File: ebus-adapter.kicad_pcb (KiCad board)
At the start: 2 copper layers, 26.7 x 45.7 mm, 27 parts, among them Q1 BC817, Q2 BC817, Q3 BC817, U1 LM358DR, U2 FODM217C, U3 FODM217C

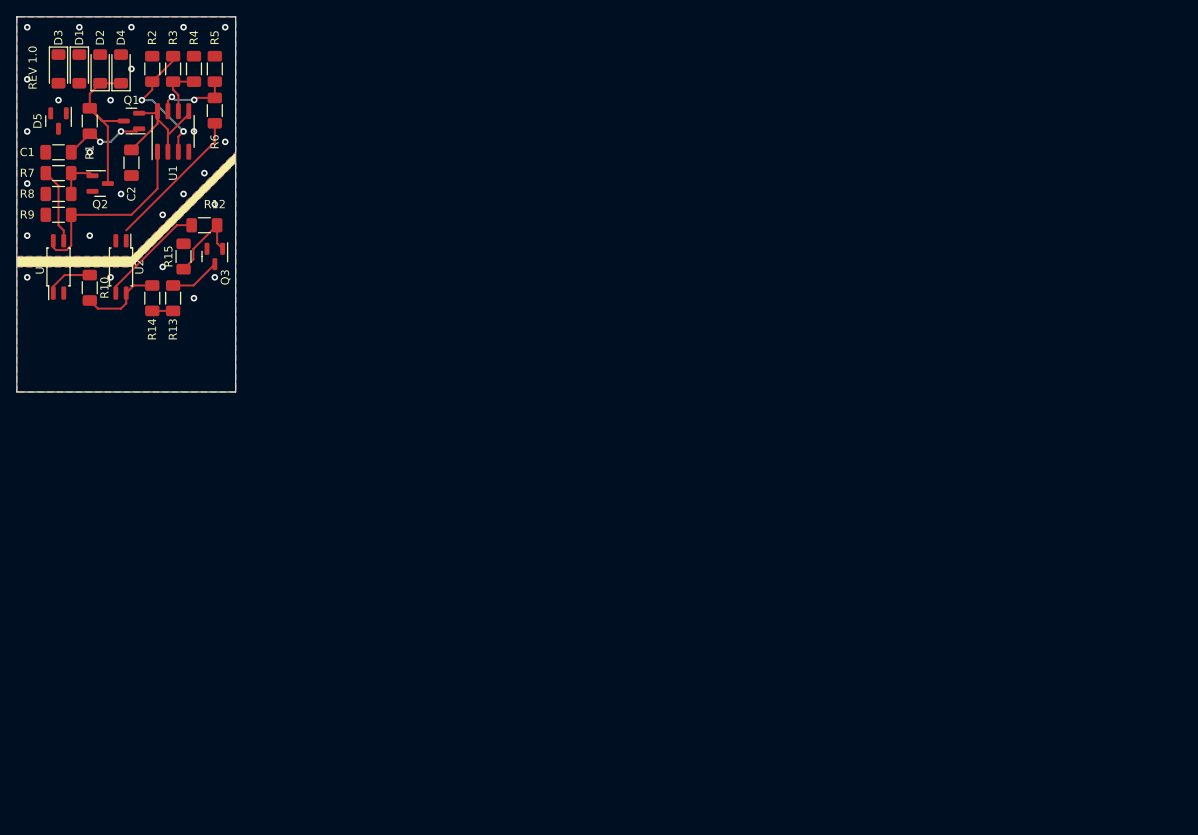
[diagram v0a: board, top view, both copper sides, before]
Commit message: Updated adapter added SPI 2 Etherenet adapter
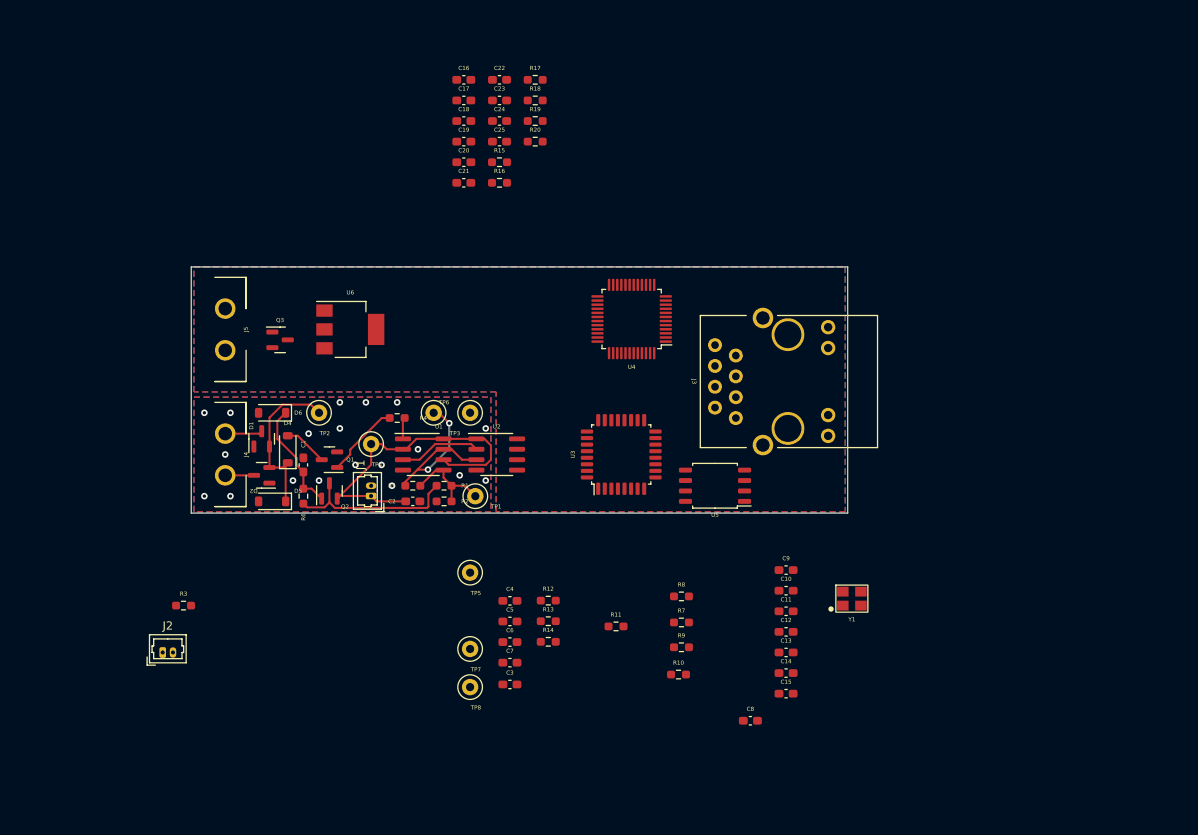
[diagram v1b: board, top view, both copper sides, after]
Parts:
- removed D3: D, Diode_SMD:D_MiniMELF
- added C10: 100u, Capacitor_SMD:C_0603_1608Metric_Pad1.08x0.95mm_HandSolder, F.Cu at (172.5, 94.1)
- added C11: 10u, Capacitor_SMD:C_0603_1608Metric_Pad1.08x0.95mm_HandSolder, F.Cu at (172.5, 96.6)
- added C12: 100p, Capacitor_SMD:C_0603_1608Metric_Pad1.08x0.95mm_HandSolder, F.Cu at (172.5, 99.1)
- added C13: 18p, Capacitor_SMD:C_0603_1608Metric_Pad1.08x0.95mm_HandSolder, F.Cu at (172.5, 101.6)
- added C14: 18p, Capacitor_SMD:C_0603_1608Metric_Pad1.08x0.95mm_HandSolder, F.Cu at (172.5, 104.1)
- added C15: 10n, Capacitor_SMD:C_0603_1608Metric_Pad1.08x0.95mm_HandSolder, F.Cu at (172.5, 106.6)
- added C16: 10n, Capacitor_SMD:C_0603_1608Metric_Pad1.08x0.95mm_HandSolder, F.Cu at (133.2, 31.8)
- added C17: 10n, Capacitor_SMD:C_0603_1608Metric_Pad1.08x0.95mm_HandSolder, F.Cu at (133.2, 34.3)
- added C18: 10u, Capacitor_SMD:C_0603_1608Metric_Pad1.08x0.95mm_HandSolder, F.Cu at (133.2, 36.8)
- added C19: 22n, Capacitor_SMD:C_0603_1608Metric_Pad1.08x0.95mm_HandSolder, F.Cu at (133.2, 39.3)
- added C20: 6.8n, Capacitor_SMD:C_0603_1608Metric_Pad1.08x0.95mm_HandSolder, F.Cu at (133.2, 41.9)
- added C21: 6.8n, Capacitor_SMD:C_0603_1608Metric_Pad1.08x0.95mm_HandSolder, F.Cu at (133.2, 44.4)
- added C22: 10n, Capacitor_SMD:C_0603_1608Metric_Pad1.08x0.95mm_HandSolder, F.Cu at (137.6, 31.8)
- added C23: 1n/2kV, Capacitor_SMD:C_0603_1608Metric_Pad1.08x0.95mm_HandSolder, F.Cu at (137.6, 34.3)
- added C24: C, Capacitor_SMD:C_0603_1608Metric_Pad1.08x0.95mm_HandSolder, F.Cu at (137.6, 36.8)
- added C25: C, Capacitor_SMD:C_0603_1608Metric_Pad1.08x0.95mm_HandSolder, F.Cu at (137.6, 39.3)
- added C3: 10u, Capacitor_SMD:C_0603_1608Metric_Pad1.08x0.95mm_HandSolder, F.Cu at (138.8, 105.5)
- added C4: 100u, Capacitor_SMD:C_0603_1608Metric_Pad1.08x0.95mm_HandSolder, F.Cu at (138.8, 95.3)
- added C5: 100p, Capacitor_SMD:C_0603_1608Metric_Pad1.08x0.95mm_HandSolder, F.Cu at (138.8, 97.8)
- added C6: 100u, Capacitor_SMD:C_0603_1608Metric_Pad1.08x0.95mm_HandSolder, F.Cu at (138.8, 100.3)
- added C7: 10u, Capacitor_SMD:C_0603_1608Metric_Pad1.08x0.95mm_HandSolder, F.Cu at (138.8, 102.8)
- added C8: 100p, Capacitor_SMD:C_0603_1608Metric_Pad1.08x0.95mm_HandSolder, F.Cu at (168.1, 109.9)
- added C9: 4.7u, Capacitor_SMD:C_0603_1608Metric_Pad1.08x0.95mm_HandSolder, F.Cu at (172.5, 91.6)
- added D6: 3.9V, Diode_SMD:D_SOD-123, F.Cu at (109.9, 72.4)
- added J1: Conn_01x02_Socket, Connector_Molex:Molex_PicoBlade_53047-0210_1x02_P1.25mm_Vertical, F.Cu at (121.9, 82.5)
- added J2: Conn_01x02_Socket, Connector_Molex:Molex_PicoBlade_53047-0210_1x02_P1.25mm_Vertical, F.Cu at (96.5, 101.6)
- added J3: HR911105A, ebus-adapter-footprints:HR911105A, F.Cu at (172.7, 68.6)
- added J4: WJ2EDGRC-5.08-2P, ebus-adapter-footprints:WJ2EDGRC, F.Cu at (104.1, 77.5)
- added J5: PWR, ebus-adapter-footprints:WJ2EDGRC, F.Cu at (104.1, 62.2)
- added R11: 0, Resistor_SMD:R_0603_1608Metric_Pad0.98x0.95mm_HandSolder, F.Cu at (151.8, 98.4)
- added R16: 49.9 1%, Resistor_SMD:R_0603_1608Metric_Pad0.98x0.95mm_HandSolder, F.Cu at (137.6, 44.4)
- added R17: 10 1%, Resistor_SMD:R_0603_1608Metric_Pad0.98x0.95mm_HandSolder, F.Cu at (141.9, 31.8)
- added R18: 49.9 1%, Resistor_SMD:R_0603_1608Metric_Pad0.98x0.95mm_HandSolder, F.Cu at (141.9, 34.3)
- added R19: 49.9 1%, Resistor_SMD:R_0603_1608Metric_Pad0.98x0.95mm_HandSolder, F.Cu at (141.9, 36.8)
- added R20: 10k, Resistor_SMD:R_0603_1608Metric_Pad0.98x0.95mm_HandSolder, F.Cu at (141.9, 39.3)
- added TP1: EBUS_RX, TestPoint:TestPoint_Loop_D1.80mm_Drill1.0mm_Beaded, F.Cu at (134.6, 82.5)
- added TP2: EBUS_SIG, TestPoint:TestPoint_Loop_D1.80mm_Drill1.0mm_Beaded, F.Cu at (115.6, 72.4)
- added TP3: EBUS_RX_LL, TestPoint:TestPoint_Loop_D1.80mm_Drill1.0mm_Beaded, F.Cu at (129.5, 72.4)
- added TP4: EBUS_3.3, TestPoint:TestPoint_Loop_D1.80mm_Drill1.0mm_Beaded, F.Cu at (121.9, 76.2)
- added TP5: BOOT0, TestPoint:TestPoint_Loop_D1.80mm_Drill1.0mm_Beaded, F.Cu at (134.0, 91.9)
- added TP6: GND1, TestPoint:TestPoint_Loop_D1.80mm_Drill1.0mm_Beaded, F.Cu at (134.0, 72.4)
- added TP7: GND2, TestPoint:TestPoint_Loop_D1.80mm_Drill1.0mm_Beaded, F.Cu at (134.0, 101.2)
- added TP8: 3.3V, TestPoint:TestPoint_Loop_D1.80mm_Drill1.0mm_Beaded, F.Cu at (134.0, 105.8)
- added U4: W5500, Package_QFP:LQFP-48_7x7mm_P0.5mm, F.Cu at (153.7, 61.0)
- added U5: W25Q128JVSIQ, Package_SO:SOIC-8_5.23x5.23mm_P1.27mm, F.Cu at (163.8, 81.3)
- added U6: AMS1117-3.3, Package_TO_SOT_SMD:SOT-223-3_TabPin2, F.Cu at (119.4, 62.2)
- added Y1: YSX321SL @24Mhz, ebus-adapter-footprints:YSX321SL, F.Cu at (180.5, 95.0)
- C1, C2: footprint Capacitor_SMD:C_1206_3216Metric_Pad1.33x1.80mm_HandSolder -> Capacitor_SMD:C_0603_1608Metric_Pad1.08x0.95mm_HandSolder
- D1, D2: value D -> BAV99; footprint Diode_SMD:D_MiniMELF -> Package_TO_SOT_SMD:SOT-23
- D4: value D -> 7.5V/1W; footprint Diode_SMD:D_MiniMELF -> Diode_SMD:D_SOD-123
- D5: value 3.9V -> 24V/1W; footprint Package_TO_SOT_SMD:SOT-23 -> Diode_SMD:D_SOD-123
- Q3: value BC817 -> DMN13H750S
- R1, R5: footprint Resistor_SMD:R_1206_3216Metric_Pad1.30x1.75mm_HandSolder -> Resistor_SMD:R_0603_1608Metric_Pad0.98x0.95mm_HandSolder
- R10, R7: value R -> 10k; footprint Resistor_SMD:R_1206_3216Metric_Pad1.30x1.75mm_HandSolder -> Resistor_SMD:R_0603_1608Metric_Pad0.98x0.95mm_HandSolder
- R12: value 1k -> 10k; footprint Resistor_SMD:R_1206_3216Metric_Pad1.30x1.75mm_HandSolder -> Resistor_SMD:R_0603_1608Metric_Pad0.98x0.95mm_HandSolder
- R13: value 1k -> 12.4k 1%; footprint Resistor_SMD:R_1206_3216Metric_Pad1.30x1.75mm_HandSolder -> Resistor_SMD:R_0603_1608Metric_Pad0.98x0.95mm_HandSolder
- R14: value 10k -> 1M; footprint Resistor_SMD:R_1206_3216Metric_Pad1.30x1.75mm_HandSolder -> Resistor_SMD:R_0603_1608Metric_Pad0.98x0.95mm_HandSolder
- R15: value 10k -> 49.9 1%; footprint Resistor_SMD:R_1206_3216Metric_Pad1.30x1.75mm_HandSolder -> Resistor_SMD:R_0603_1608Metric_Pad0.98x0.95mm_HandSolder
- R2: value 173k -> 33k; footprint Resistor_SMD:R_1206_3216Metric_Pad1.30x1.75mm_HandSolder -> Resistor_SMD:R_0603_1608Metric_Pad0.98x0.95mm_HandSolder
- R3: value 33k -> R; footprint Resistor_SMD:R_1206_3216Metric_Pad1.30x1.75mm_HandSolder -> Resistor_SMD:R_0603_1608Metric_Pad0.98x0.95mm_HandSolder
- R4: value 67k -> 4k7; footprint Resistor_SMD:R_1206_3216Metric_Pad1.30x1.75mm_HandSolder -> Resistor_SMD:R_0603_1608Metric_Pad0.98x0.95mm_HandSolder
- R6: value R -> 100k; footprint Resistor_SMD:R_1206_3216Metric_Pad1.30x1.75mm_HandSolder -> Resistor_SMD:R_0603_1608Metric_Pad0.98x0.95mm_HandSolder
- R8, R9: value R -> 330; footprint Resistor_SMD:R_1206_3216Metric_Pad1.30x1.75mm_HandSolder -> Resistor_SMD:R_0603_1608Metric_Pad0.98x0.95mm_HandSolder
- U2: value FODM217C -> ADuM1201BR; footprint Package_SO:SOP-4_4.4x2.6mm_P1.27mm -> Package_SO:SOIC-8_3.9x4.9mm_P1.27mm
- U3: value FODM217C -> STM32L412KBTx; footprint Package_SO:SOP-4_4.4x2.6mm_P1.27mm -> Package_QFP:LQFP-32_7x7mm_P0.8mm
- moved R7 93.6 mm to (159.7, 97.9), turned to 0 degrees
- moved R9 92.4 mm to (159.7, 101.0), turned to 0 degrees
- moved R8 90.4 mm to (159.7, 94.8)
- moved R10 85.9 mm to (159.4, 104.3), turned to 0 degrees
- moved U3 72.3 mm to (152.4, 77.5)
- moved R3 65.4 mm to (99.1, 95.9), turned to 0 degrees
- moved R14 63.9 mm to (143.5, 100.3), turned to 0 degrees
- moved R2 63.6 mm to (130.8, 83.2), turned to 180 degrees
- moved R12 62.0 mm to (143.5, 95.3), turned to 0 degrees
- moved R1 62.0 mm to (130.8, 81.3), turned to 0 degrees
- moved R13 60.3 mm to (143.5, 97.8), turned to 0 degrees
- moved R5 56.2 mm to (127.0, 81.3), turned to 180 degrees
- moved C2 53.7 mm to (127.0, 83.2), turned to 0 degrees
- moved D2 53.3 mm to (108.6, 80.0), turned to 180 degrees
- moved D5 53.2 mm to (109.9, 83.2), turned to 180 degrees
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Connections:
- C1 pad 1: Net-(D5-K) -> Net-(D6-K)
- C1 pad 2: GNDPWR -> GND1
- C2 pad 1: EBUS_3.3_VREF -> /EBUS_3.3V
- C2 pad 2: GNDPWR -> GND1
- D1 pad 1: /Ebus-To-UART/EBUS1 -> GND1
- D1 pad 2: GNDPWR -> /EBUS_SIGNAL
- D2 pad 1: EBUS_SIGNAL -> GND1
- D2 pad 2: /Ebus-To-UART/EBUS1 -> /EBUS_SIGNAL
- D4 pad 1: EBUS_SIGNAL -> /EBUS_SIGNAL
- D4 pad 2: /Ebus-To-UART/EBUS2 -> Net-(D4-A)
- D5 pad 1: Net-(D5-K) -> /EBUS_SIGNAL
- D5 pad 2: GNDPWR -> GND1
- Q1 pad 1: Net-(D5-K) -> Net-(Q1-B)
- Q1 pad 2: EBUS_3.3_VREF -> GND1
- Q1 pad 3: EBUS_SIGNAL -> Net-(D4-A)
- Q2 pad 1: Net-(Q2-B) -> Net-(D6-K)
- Q2 pad 2: GNDPWR -> /EBUS_3.3V
- Q2 pad 3: EBUS_SIGNAL -> /EBUS_SIGNAL
- Q3 pad 1: Net-(Q3-B) -> GND2
- Q3 pad 2: GND -> Net-(Q3-S)
- Q3 pad 3: Net-(Q3-C) -> Net-(J5-In)
- R1 pad 1: EBUS_SIGNAL -> /EBUS_SIGNAL
- R1 pad 2: Net-(D5-K) -> Net-(U1B-+)
- R10 pad 1: Net-(R10-Pad1) -> +3.3V
- R10 pad 2: +3.3V -> /NRST_MCU
- R12 pad 1: Net-(Q3-B) -> +3.3V
- R12 pad 2: Net-(R12-Pad2) -> Net-(U4-PMODE0)
- R13 pad 1: /Ebus-To-UART/RX -> Net-(U4-EXRES1)
- R13 pad 2: Net-(Q3-C) -> GND2
- R14 pad 1: +3.3V -> Net-(U4-XI/CLKIN)
- R14 pad 2: /Ebus-To-UART/RX -> Net-(U4-XO)
- R15 pad 1: Net-(Q3-B) -> +3.3VA
- R15 pad 2: GND -> /TX-
- R2 pad 1: EBUS_SIGNAL -> Net-(U1B-+)
- R2 pad 2: Net-(U1A-+) -> GND1
- R3 pad 1: Net-(U1A-+) -> /_EBUS_PWR
- R3 pad 2: Net-(U1B--) -> Net-(D3-A)
- R4 pad 1: Net-(U1B--) -> Net-(R4-Pad1)
- R4 pad 2: GNDPWR -> Net-(Q1-B)
- R5 pad 1: Net-(U1B--) -> Net-(U1B-+)
- R5 pad 2: Net-(R5-Pad2) -> /VIB
- R6 pad 1: Net-(R5-Pad2) -> /EBUS_SIGNAL
- R6 pad 2: Net-(R6-Pad2) -> Net-(D6-K)
- R7 pad 1: Net-(Q2-B) -> +3.3V
- R7 pad 2: Net-(R7-Pad2) -> /NRST
- R8 pad 1: GNDPWR -> +3.3V
- R8 pad 2: Net-(Q2-B) -> Net-(J3-GLED-)
- R9 pad 1: Net-(R9-Pad1) -> Net-(J3-YLED-)
- R9 pad 2: GNDPWR -> +3.3V
- U1 pad 1: Net-(R9-Pad1) -> Net-(R4-Pad1)
- U1 pad 2: EBUS_3.3_VREF -> /EBUS_3.3V
- U1 pad 3: Net-(U1A-+) -> /VOA
- U1 pad 4: GNDPWR -> GND1
- U1 pad 5: EBUS_3.3_VREF -> Net-(U1B-+)
- U1 pad 6: Net-(U1B--) -> /EBUS_3.3V
- U1 pad 7: Net-(R5-Pad2) -> /VIB
- U1 pad 8: EBUS_3.3_VREF -> /EBUS_3.3V
- U2 pad 1: Net-(R6-Pad2) -> /EBUS_3.3V
- U2 pad 2: GNDPWR -> /VOA
- U2 pad 3: Net-(R12-Pad2) -> /VIB
- U2 pad 4: +3.3V -> GND1
- U3 pad 1: Net-(R10-Pad1) -> +3.3V
- U3 pad 2: /Ebus-To-UART/TX -> unconnected-(U3-PC14-Pad2)
- U3 pad 3: Net-(R7-Pad2) -> unconnected-(U3-PC15-Pad3)
- U3 pad 4: Net-(R9-Pad1) -> /NRST
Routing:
- net /EBUS_SIGNAL: track 0.00 -> 41.8 mm
- net /EBUS_3.3V: track 0.00 -> 40.9 mm
- net Net-(R9-Pad1): track 23.4 -> 0.00 mm
- net /VIB: track 0.00 -> 21.7 mm, vias 0 -> 2
- net EBUS_SIGNAL: track 21.0 -> 0.00 mm
- net EBUS_3.3_VREF: track 19.9 -> 0.00 mm
- net Net-(R6-Pad2): track 17.5 -> 0.00 mm
- net Net-(U1A-+): track 16.3 -> 0.00 mm, vias 2 -> 0
- net Net-(D6-K): track 0.00 -> 13.7 mm
- net Net-(R12-Pad2): track 13.1 -> 0.00 mm
- net Net-(U1B-+): track 0.00 -> 11.3 mm
- net Net-(D5-K): track 10.3 -> 0.00 mm, vias 2 -> 0
- net Net-(Q3-B): track 10.2 -> 0.00 mm
- net /VOA: track 0.00 -> 10.0 mm
- net +3.3V: track 9.93 -> 0.00 mm
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- added copper zone on B.Cu, net GND1
- added copper zone on F.Cu, net GND1
- added copper zone on B.Cu, net GND2
- added copper zone on F.Cu, net GND2
- removed copper zone on B.Cu, net GND
- removed copper zone on F.Cu, net GND
- removed copper zone on B.Cu, net GNDPWR
- removed copper zone on F.Cu, net GNDPWR
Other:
- board size 26.7 x 45.7 mm -> 80 x 30 mm
- board text removed: "REV 1.0"

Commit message: Updated schematics and pcb
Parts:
- removed C14: 18p, Capacitor_SMD:C_0603_1608Metric_Pad1.08x0.95mm_HandSolder
- removed C15, C22: 10n, Capacitor_SMD:C_0603_1608Metric_Pad1.08x0.95mm_HandSolder
- removed C19: 22n, Capacitor_SMD:C_0603_1608Metric_Pad1.08x0.95mm_HandSolder
- removed C20, C21: 6.8n, Capacitor_SMD:C_0603_1608Metric_Pad1.08x0.95mm_HandSolder
- removed R19: 49.9 1%, Resistor_SMD:R_0603_1608Metric_Pad0.98x0.95mm_HandSolder
- added D3: LED, LED_THT:LED_D1.8mm_W3.3mm_H2.4mm, F.Cu at (203.2, 73.7)
- added D7: LED, LED_THT:LED_D1.8mm_W3.3mm_H2.4mm, F.Cu at (210.8, 85.7)
- added FB1: 120 Ohm @ 100 MHz, Resistor_SMD:R_1206_3216Metric_Pad1.30x1.75mm_HandSolder, F.Cu at (129.8, 116.8)
- added FB2: 120 Ohm @ 100 MHz, Resistor_SMD:R_1206_3216Metric_Pad1.30x1.75mm_HandSolder, F.Cu at (148.4, 118.6)
- added J6: Conn_01x05_Pin, Connector_PinHeader_2.54mm:PinHeader_1x05_P2.54mm_Vertical, F.Cu at (113.7, 90.8)
- added J7: Conn_01x02_Socket, Connector_Molex:Molex_PicoBlade_53047-0210_1x02_P1.25mm_Vertical, F.Cu at (156.8, 92.7)
- added J8: Conn_01x02_Socket, Connector_Molex:Molex_PicoBlade_53047-0210_1x02_P1.25mm_Vertical, F.Cu at (217.8, 84.5)
- added SW2: PS-7054SVB-6PN, ebus-adapter-footprints:PS-7054SVB, F.Cu at (121.3, 97.2)
- C6: value 100u -> 10uF
- C7: value 10u -> 0.1uF
- C8: value 100p -> 0.1uF
- C9: value 4.7u -> 18p
- R12: value 10k -> 2.32k 1%
- R13: value 12.4k 1% -> 49.9 1%
- R14: value 1M -> 49.9 1%
- R17: value 10 1% -> 1M
- R18: value 49.9 1% -> R
- TP1, TP2, TP3, TP4, TP5, TP6, TP7, TP8: footprint TestPoint:TestPoint_Loop_D1.80mm_Drill1.0mm_Beaded -> TestPoint:TestPoint_THTPad_1.5x1.5mm_Drill0.7mm
- U4: value W5500 -> ENC28J60x-ML; footprint Package_QFP:LQFP-48_7x7mm_P0.5mm -> Package_DFN_QFN:QFN-28-1EP_6x6mm_P0.65mm_EP4.25x4.25mm
- Y1: value YSX321SL @24Mhz -> YSX321SL @25Mhz
- moved J2 112.2 mm to (204.1, 69.4)
- moved C17 81.3 mm to (133.0, 115.6)
- moved C18 80.6 mm to (133.0, 117.5)
- moved R17 73.1 mm to (137.2, 104.8), turned to -90 degrees
- moved R15 71.5 mm to (149.2, 112.4), turned to 180 degrees
- moved R16 71.1 mm to (149.2, 114.5), turned to 180 degrees
- moved C24 70.7 mm to (106.0, 100.1)
- moved C23 69.5 mm to (149.2, 102.9), turned to 180 degrees
- moved C16 68.7 mm to (143.5, 99.7), turned to 180 degrees
- moved C25 66.8 mm to (106.0, 98.2), turned to 180 degrees
- moved R18 64.4 mm to (155.9, 97.2)
- moved R20 63.7 mm to (128.3, 101.6), turned to -90 degrees
- moved TP6 56.0 mm to (103.5, 119.4)
- moved U4 52.1 mm to (142.2, 111.8), turned to 90 degrees
- moved C10 51.7 mm to (126.4, 117.5), turned to 180 degrees
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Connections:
- C13 pad 1: Net-(U4-XI/CLKIN) -> Net-(C13-Pad1)
- C6 pad 1: +3.3V -> Net-(U4-VCAP)
- C7 pad 1: +3.3V -> GND2
- C7 pad 2: GND2 -> Net-(J3-TCT)
- C8 pad 1: +3.3V -> GND2
- C8 pad 2: GND2 -> Net-(J3-RCT)
- C9 pad 1: Net-(U4-TOCAP) -> Net-(U4-OSC1)
- J1 pad 1: /EBUS_3.3V -> Net-(J1-Pin_1)
- J3 pad 3: Net-(J3-RXD+) -> /RX+
- J3 pad 6: Net-(J3-RXD-) -> /RX-
- R12 pad 1: +3.3V -> Net-(U4-RBIAS)
- R12 pad 2: Net-(U4-PMODE0) -> GND2
- R13 pad 1: Net-(U4-EXRES1) -> Net-(J3-RCT)
- R13 pad 2: GND2 -> /RX+
- R14 pad 1: Net-(U4-XI/CLKIN) -> Net-(J3-RCT)
- R14 pad 2: Net-(U4-XO) -> /RX-
- R15 pad 1: +3.3VA -> Net-(J3-TCT)
- R15 pad 2: /TX- -> /TX+
- R16 pad 1: +3.3VA -> Net-(J3-TCT)
- R16 pad 2: /TX+ -> /TX-
- R17 pad 1: +3.3VA -> Net-(C13-Pad1)
- R17 pad 2: Net-(J3-TCT) -> Net-(U4-OSC2)
- R18 pad 1: /RX+ -> /ACT
- R18 pad 2: Net-(J3-RCT) -> Net-(J7-Pin_1)
- R3 pad 1: /_EBUS_PWR -> /EBUS_3.3V
- R3 pad 2: Net-(D3-A) -> Net-(J1-Pin_1)
- U3 pad 10: unconnected-(U3-PA4-Pad10) -> /ACT
- U3 pad 21: /SPI_MISO -> /ETHER_DI
- U3 pad 22: /SPI_MOSI -> /ETHER_DO
- U3 pad 7: /SPI_SCK -> /ETHER_SCK
- U4 pad 1: /TX- -> unconnected-(U4-~{WOL}-Pad1)
- U4 pad 10: Net-(U4-EXRES1) -> Net-(U4-RBIAS)
- U4 pad 12: unconnected-(U4-NC-Pad12) -> /RX-
- U4 pad 13: unconnected-(U4-NC-Pad13) -> /RX+
- U4 pad 16: GND2 -> +3.3VA
- U4 pad 17: +3.3VA -> GND2
- U4 pad 18: unconnected-(U4-VBG-Pad18) -> GND2
- U4 pad 19: GND2 -> Net-(U4-OSC1)
- U4 pad 2: /TX+ -> /ETHER_DI
- U4 pad 20: Net-(U4-TOCAP) -> Net-(U4-OSC2)
- U4 pad 22: Net-(U4-1V2O) -> /SPD_LED
- U4 pad 23: GND2 -> /LNK_LED
- U4 pad 24: /SPD_LED -> +3.3VA
- U4 pad 25: /LNK_LED -> Net-(U4-VCAP)
- U4 pad 26: unconnected-(U4-DUPLED-Pad26) -> GND2
- U4 pad 28: GND2 -> /ETHER_INT
- U4 pad 29: GND2 -> (no net)
- U4 pad 3: GND2 -> /ETHER_DO
- U4 pad 4: +3.3VA -> /ETHER_SCK
- U4 pad 5: /RX- -> /ETHER_CS
- U4 pad 6: /RX+ -> /NRST_MCU
- U4 pad 7: unconnected-(U4-DNC-Pad7) -> GND2
- U4 pad 8: +3.3VA -> /TX-
- U4 pad 9: GND2 -> /TX+
- U5 pad 8: GND2 -> +3.3V
- Y1 pad 1: Net-(U4-XI/CLKIN) -> Net-(U4-OSC1)
- Y1 pad 3: Net-(U4-XO) -> Net-(C13-Pad1)
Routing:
- net /NRST_MCU: track 0.00 -> 52.9 mm, vias 0 -> 2
- net +3.3V: track 0.00 -> 43.9 mm, vias 0 -> 16
- net /ETHER_CS: track 0.00 -> 40.3 mm, vias 0 -> 2
- net /ETHER_DO: track 0.00 -> 38.3 mm, vias 0 -> 2
- net /ETHER_DI: track 0.00 -> 36.3 mm, vias 0 -> 2
- net /SPD_LED: track 0.00 -> 34.6 mm, vias 0 -> 1
- net /LNK_LED: track 0.00 -> 34.3 mm, vias 0 -> 1
- net /ETHER_INT: track 0.00 -> 33.6 mm, vias 0 -> 2
- net /ETHER_SCK: track 0.00 -> 28.4 mm, vias 0 -> 2
- net /RX: track 0.00 -> 26.5 mm, vias 0 -> 2
- net /SWDIO: track 0.00 -> 23.6 mm
- net /TX: track 0.00 -> 23.5 mm, vias 0 -> 2
- net /EBUS_3.3V: track 40.9 -> 18.8 mm, vias 0 -> 4
- net /SWCLK: track 0.00 -> 21.5 mm
- net Net-(U1B-+): track 11.3 -> 31.4 mm, vias 0 -> 1
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- added copper zone on F.Cu, net +3.3V
- added copper zone on In2.Cu, net +3.3V
- added copper zone on In2.Cu, net +3.3VA
- added copper zone on In2.Cu, net /EBUS_3.3V
- added copper zone on In1.Cu, net GND1
- added copper zone on In1.Cu, net GND2
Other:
- board size 80 x 30 mm -> 86.9 x 32.8 mm
- copper layers 2 -> 4
- board text added: "EBUS"
- board text added: "PWR -+ 5-12V"
